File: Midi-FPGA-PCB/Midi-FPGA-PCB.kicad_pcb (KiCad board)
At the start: 4 copper layers, 4 parts

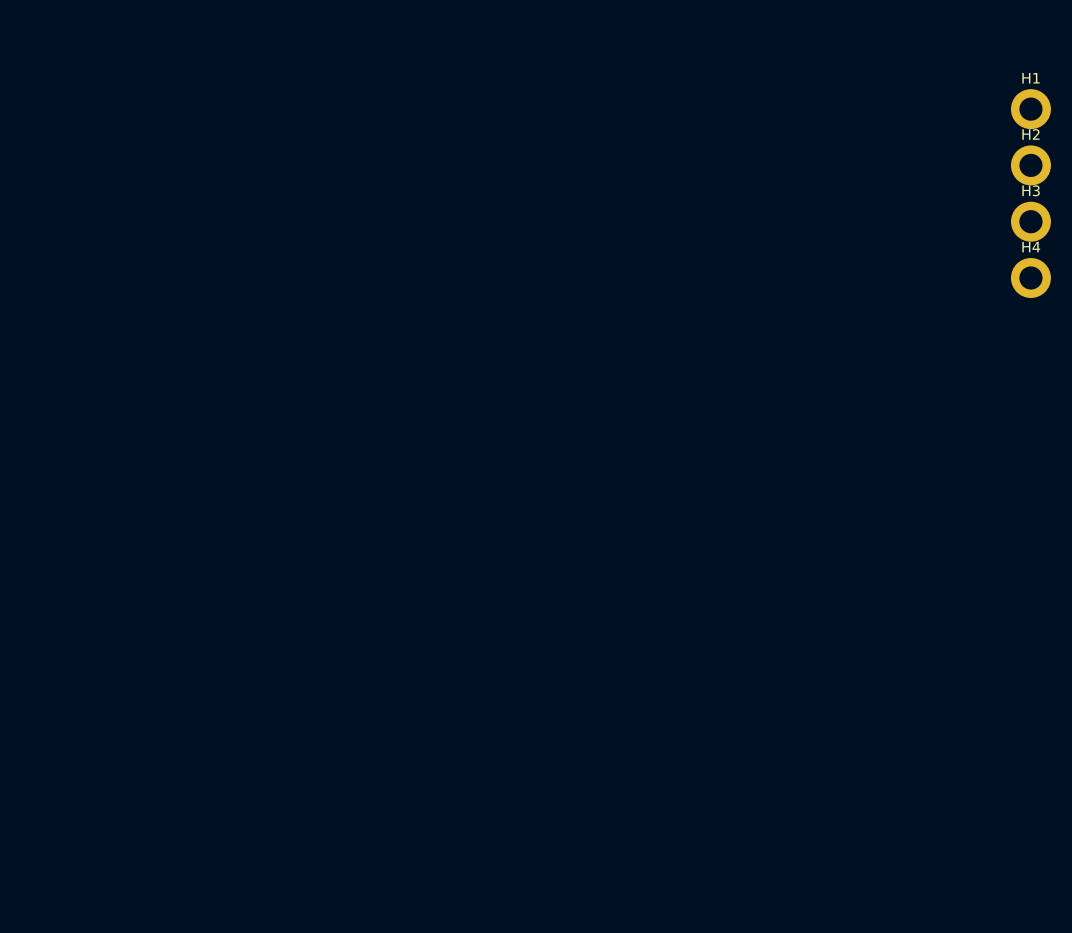
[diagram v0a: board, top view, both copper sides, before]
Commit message: Created board outline
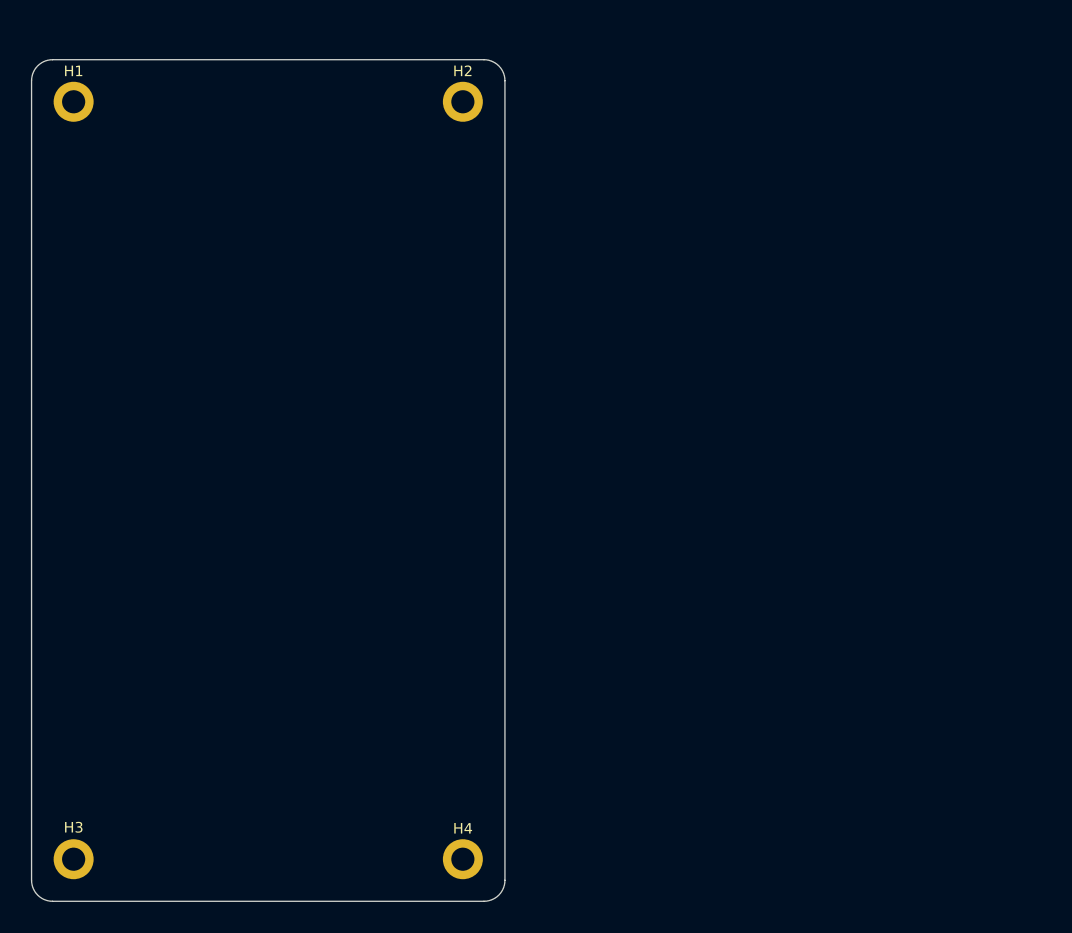
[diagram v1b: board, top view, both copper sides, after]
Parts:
- moved H3 109.3 mm to (99.0, 141.0)
- moved H1 91.0 mm to (99.0, 69.0)
- moved H4 77.3 mm to (136.0, 141.0)
- moved H2 54.3 mm to (136.0, 69.0)
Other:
- board outline added: 45 x 80 mm
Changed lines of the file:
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@@
   (net 1 "GND")
   (footprint "MountingHole:MountingHole_2.2mm_M2_DIN965_Pad" (layer "F.Cu")
-    (at 190 85.75)
+    (at 136 141)
     (descr "Mounting Hole 2.2mm, M2, DIN965")
     (tags "mounting hole 2.2mm m2 din965")
@@
   )
   (footprint "MountingHole:MountingHole_2.2mm_M2_DIN965_Pad" (layer "F.Cu")
-    (at 190 80.4)
+    (at 99 141)
     (descr "Mounting Hole 2.2mm, M2, DIN965")
     (tags "mounting hole 2.2mm m2 din965")
@@
     (property "ki_keywords" "mounting hole")
     (attr exclude_from_pos_files)
-    (fp_text reference "H3" (at 0 -2.9) (layer "F.SilkS")
+    (fp_text reference "H3" (at 0 -3) (layer "F.SilkS")
         (effects (font (size 1 1) (thickness 0.15)))
     )
@@
   )
   (footprint "MountingHole:MountingHole_2.2mm_M2_DIN965_Pad" (layer "F.Cu")
-    (at 190 69.7)
+    (at 99 69)
     (descr "Mounting Hole 2.2mm, M2, DIN965")
     (tags "mounting hole 2.2mm m2 din965")
@@
   )
   (footprint "MountingHole:MountingHole_2.2mm_M2_DIN965_Pad" (layer "F.Cu")
-    (at 190 75.05)
+    (at 136 69)
     (descr "Mounting Hole 2.2mm, M2, DIN965")
     (tags "mounting hole 2.2mm m2 din965")
@@
       (net 1 "GND") (pinfunction "1") (pintype "input"))
   )
+  (gr_line (start 140 67) (end 140 143)
+    (stroke (width 0.1) (type default)) (layer "Edge.Cuts"))
+  (gr_line (start 138 145) (end 97 145)
+    (stroke (width 0.1) (type default)) (layer "Edge.Cuts"))
+  (gr_arc (start 140 143) (mid 139.414214 144.414214) (end 138 145)
+    (stroke (width 0.1) (type default)) (layer "Edge.Cuts"))
+  (gr_arc (start 138 65) (mid 139.414214 65.585786) (end 140 67)
+    (stroke (width 0.1) (type default)) (layer "Edge.Cuts"))
+  (gr_arc (start 95 67) (mid 95.585786 65.585786) (end 97 65)
+    (stroke (width 0.1) (type default)) (layer "Edge.Cuts"))
+  (gr_line (start 95 143) (end 95 67)
+    (stroke (width 0.1) (type default)) (layer "Edge.Cuts"))
+  (gr_line (start 97 65) (end 138 65)
+    (stroke (width 0.1) (type default)) (layer "Edge.Cuts"))
+  (gr_arc (start 97 145) (mid 95.585786 144.414214) (end 95 143)
+    (stroke (width 0.1) (type default)) (layer "Edge.Cuts"))
 )

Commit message: Added ground plane fill
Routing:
- added copper zone on In1.Cu, net GND
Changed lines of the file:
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@@
   (gr_arc (start 97 145) (mid 95.585786 144.414214) (end 95 143)
     (stroke (width 0.1) (type default)) (layer "Edge.Cuts"))
+  (zone (net 1) (net_name "GND") (layer "In1.Cu") (name "Ground plane") (hatch edge 0.5)
+    (connect_pads (clearance 0.5))
+    (min_thickness 0.25) (filled_areas_thickness no)
+    (fill (thermal_gap 0.5) (thermal_bridge_width 0.5))
+    (polygon
+      (pts
+        (xy 80 60)
+        (xy 150 60)
+        (xy 150 150)
+        (xy 80 150)
+      )
+    )
+  )
 )

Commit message: Added title, date and revision to pcb
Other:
- board text added: "1.0.0"
- board text added: "Midi FPGA"
- board text added: "November 2023"
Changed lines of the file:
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@@
   (gr_arc (start 97 145) (mid 95.585786 144.414214) (end 95 143)
     (stroke (width 0.1) (type default)) (layer "Edge.Cuts"))
+  (gr_text "Midi FPGA" (at 186 190.5) (layer "Cmts.User")
+    (effects (font (size 2 2) (thickness 0.2)) (justify left bottom))
+  )
+  (gr_text "November 2023" (at 206 194) (layer "Cmts.User")
+    (effects (font (size 1.5 1.5) (thickness 0.15)) (justify left bottom))
+  )
+  (gr_text "1.0.0" (at 268 194) (layer "Cmts.User")
+    (effects (font (size 1.5 1.5) (thickness 0.15)) (justify left bottom))
+  )
   (zone (net 1) (net_name "GND") (layer "In1.Cu") (name "Ground plane") (hatch edge 0.5)
     (connect_pads (clearance 0.5))

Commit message: ESP32 placement
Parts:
- added U1: ESP32-WROOM-32, Midi-FPGA-lib:ESP32-WROOM-32 (No Thermal), F.Cu at (117.5, 81.2)

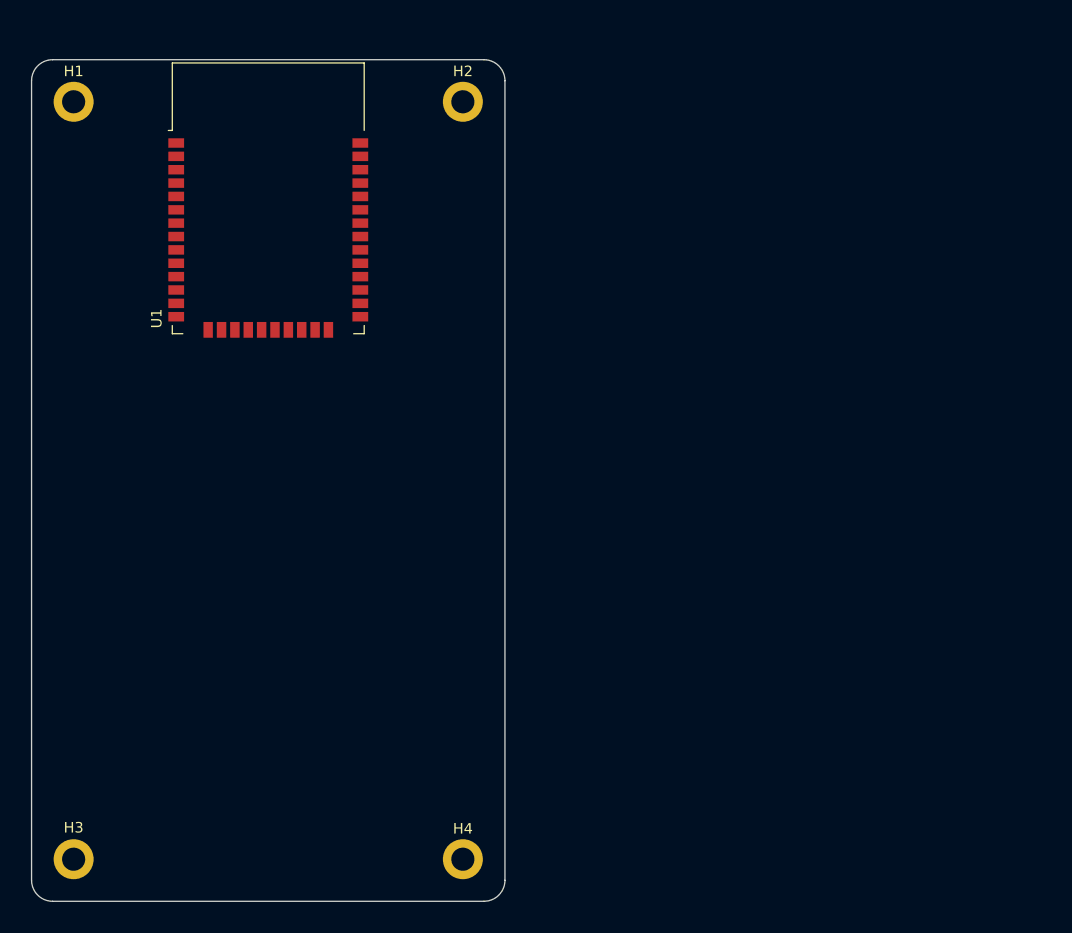
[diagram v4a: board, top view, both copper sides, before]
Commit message: Added ground fills
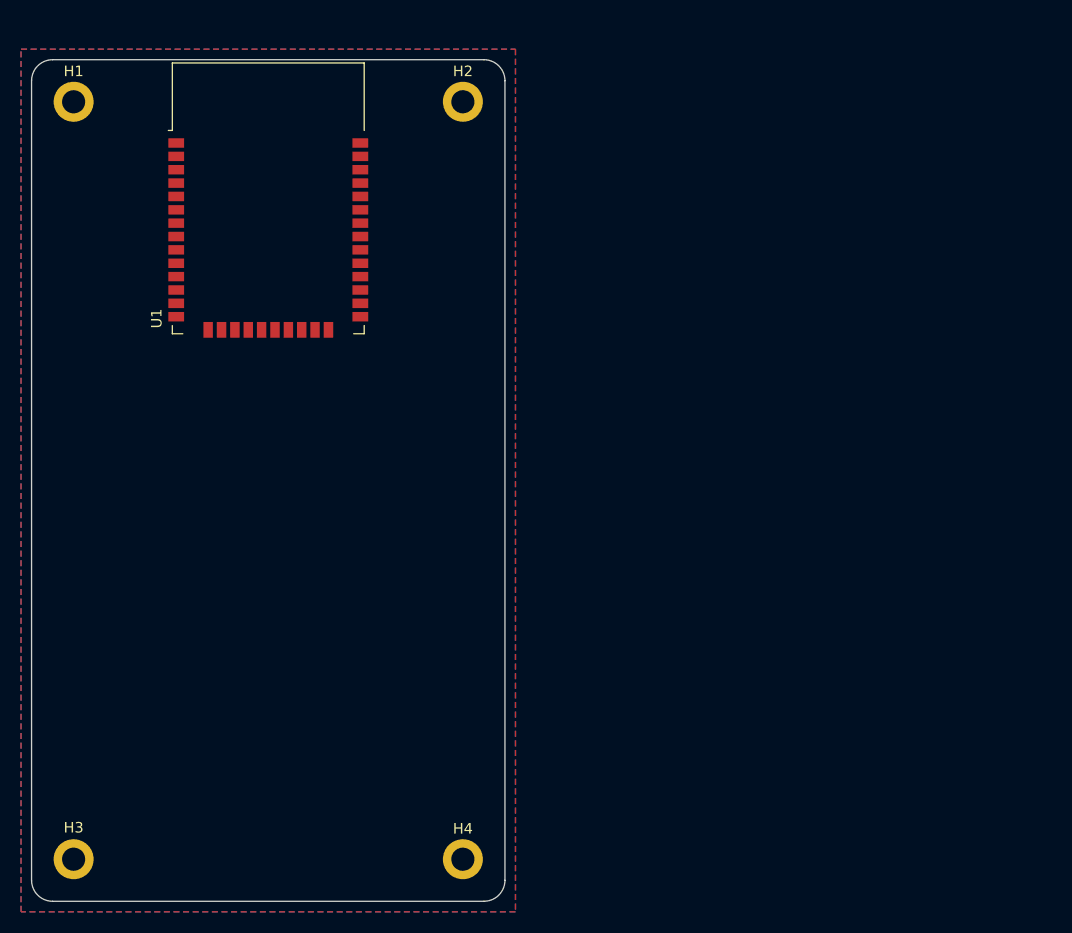
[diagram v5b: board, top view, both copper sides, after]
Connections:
- U1 pad 1: Net-(U1-GND-Pad1) -> GND
- U1 pad 15: Net-(U1-GND-Pad1) -> GND
- U1 pad 38: Net-(U1-GND-Pad1) -> GND
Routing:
- added copper zone on B.Cu, net GND
- added copper zone on F.Cu, net GND

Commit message: Added USB circuit
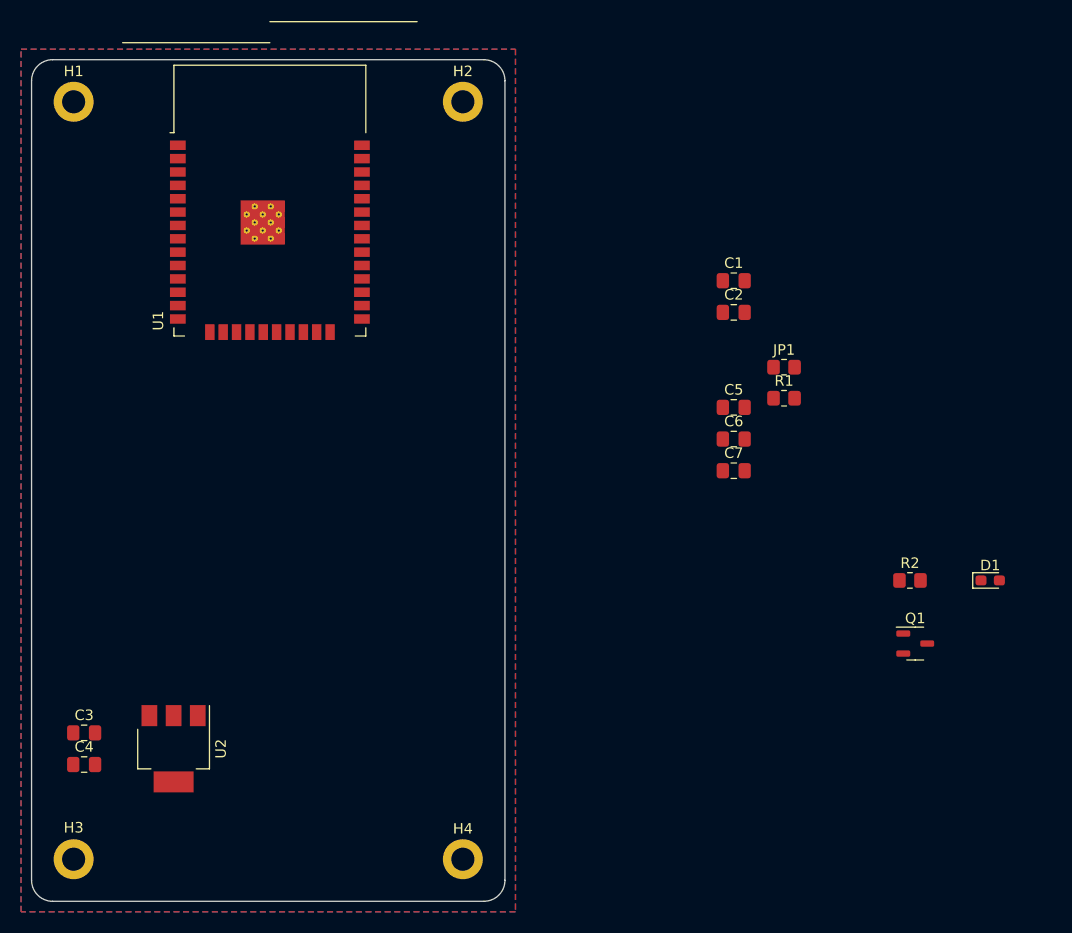
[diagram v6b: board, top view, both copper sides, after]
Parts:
- added C1: 22uF, Capacitor_SMD:C_0805_2012Metric_Pad1.18x1.45mm_HandSolder, F.Cu at (161.8, 86.0)
- added C2: 0.1uF, Capacitor_SMD:C_0805_2012Metric_Pad1.18x1.45mm_HandSolder, F.Cu at (161.8, 89.0)
- added C3: 4.7uF, Capacitor_SMD:C_0805_2012Metric_Pad1.18x1.45mm_HandSolder, F.Cu at (100.0, 129.0)
- added C4: 4.7uF, Capacitor_SMD:C_0805_2012Metric_Pad1.18x1.45mm_HandSolder, F.Cu at (100.0, 132.0)
- added C5: 0.1uF, Capacitor_SMD:C_0805_2012Metric_Pad1.18x1.45mm_HandSolder, F.Cu at (161.8, 98.0)
- added C6: 0.1uF, Capacitor_SMD:C_0805_2012Metric_Pad1.18x1.45mm_HandSolder, F.Cu at (161.8, 101.1)
- added C7: 1uF, Capacitor_SMD:C_0805_2012Metric_Pad1.18x1.45mm_HandSolder, F.Cu at (161.8, 104.1)
- added D1: LED, LED_SMD:LED_0603_1608Metric_Pad1.05x0.95mm_HandSolder, F.Cu at (186.1, 114.5)
- added JP1: 0, Resistor_SMD:R_0805_2012Metric_Pad1.20x1.40mm_HandSolder, F.Cu at (166.5, 94.2)
- added Q1: DMP2123L, Package_TO_SOT_SMD:SOT-23-3, F.Cu at (179.0, 120.5)
- added R1: 10K, Resistor_SMD:R_0805_2012Metric_Pad1.20x1.40mm_HandSolder, F.Cu at (166.5, 97.2)
- added R2: 150, Resistor_SMD:R_0805_2012Metric_Pad1.20x1.40mm_HandSolder, F.Cu at (178.5, 114.5)
- added U2: AP7361EA, Midi-FPGA-lib:SOT-223-3R, F.Cu at (108.5, 130.5)
- U1: footprint Midi-FPGA-lib:ESP32-WROOM-32 (No Thermal) -> Midi-FPGA-lib:ESP32-WROOM-32
- moved U1 0.27 mm to (117.7, 81.4)
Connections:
- U1 pad 2: unconnected-(U1-VDD-Pad2) -> VDD
- U1 pad 25: unconnected-(U1-IO0-Pad25) -> Boot
- U1 pad 3: unconnected-(U1-EN-Pad3) -> EN
- U1 pad 6: unconnected-(U1-IO34-Pad6) -> RX
- U1 pad 7: unconnected-(U1-IO35-Pad7) -> TX

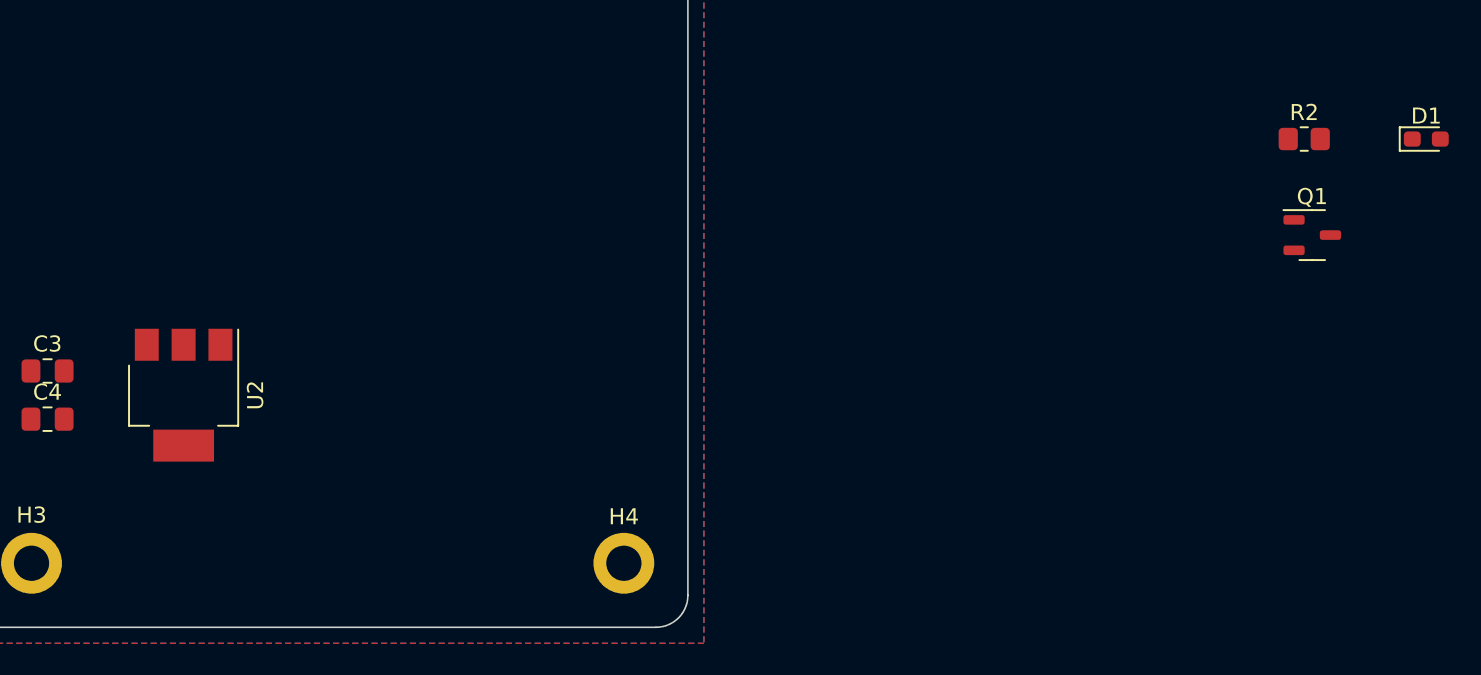
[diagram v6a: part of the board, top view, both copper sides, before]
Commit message: Added custom usb c library
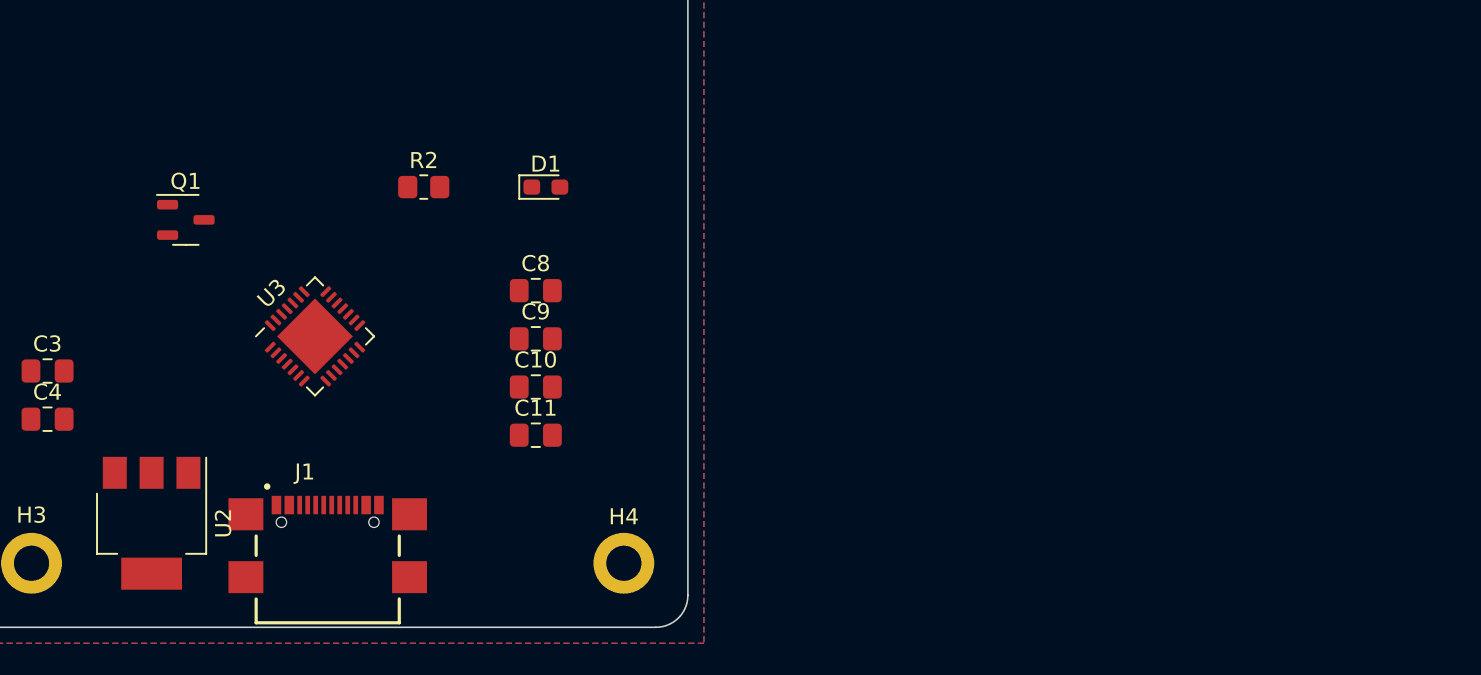
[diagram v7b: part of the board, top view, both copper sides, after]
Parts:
- added C10: 4.7uF, Capacitor_SMD:C_0805_2012Metric_Pad1.18x1.45mm_HandSolder, F.Cu at (130.5, 130.0)
- added C11: 0.1uF, Capacitor_SMD:C_0805_2012Metric_Pad1.18x1.45mm_HandSolder, F.Cu at (130.5, 133.0)
- added C8: 1uF, Capacitor_SMD:C_0805_2012Metric_Pad1.18x1.45mm_HandSolder, F.Cu at (130.5, 124.0)
- added C9: 0.1uF, Capacitor_SMD:C_0805_2012Metric_Pad1.18x1.45mm_HandSolder, F.Cu at (130.5, 127.0)
- added J1: USB4110GFA, USB4110_GF_A:GCT_USB4110GFA, F.Cu at (117.5, 138.4)
- added U3: CP2102N-Axx-xQFN28, Package_DFN_QFN:QFN-28-1EP_5x5mm_P0.5mm_EP3.35x3.35mm, F.Cu at (116.7, 126.8)
- moved Q1 70.4 mm to (108.6, 119.5)
- moved D1 55.1 mm to (131.1, 117.5)
- moved R2 55.1 mm to (123.5, 117.5)
- moved U2 8.25 mm to (106.5, 138.5)
